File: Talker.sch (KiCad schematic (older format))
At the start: 61 parts, among them J1 DC_JACK, J2 DE9, J3 Audio Out, J4 TxE, J5 SPKR, J6 32/16, P1 10K, SW1 RESET, U1 CTS256A-AL2, U10 2732, U11 6116, U2 74ALS573, U3 74LS138, U4 SP0256A-AL2, U5 LM324, U6 LM386, U7 MAX232, U8 74LS14, Y1 10MHz, Y2 3.12MHz

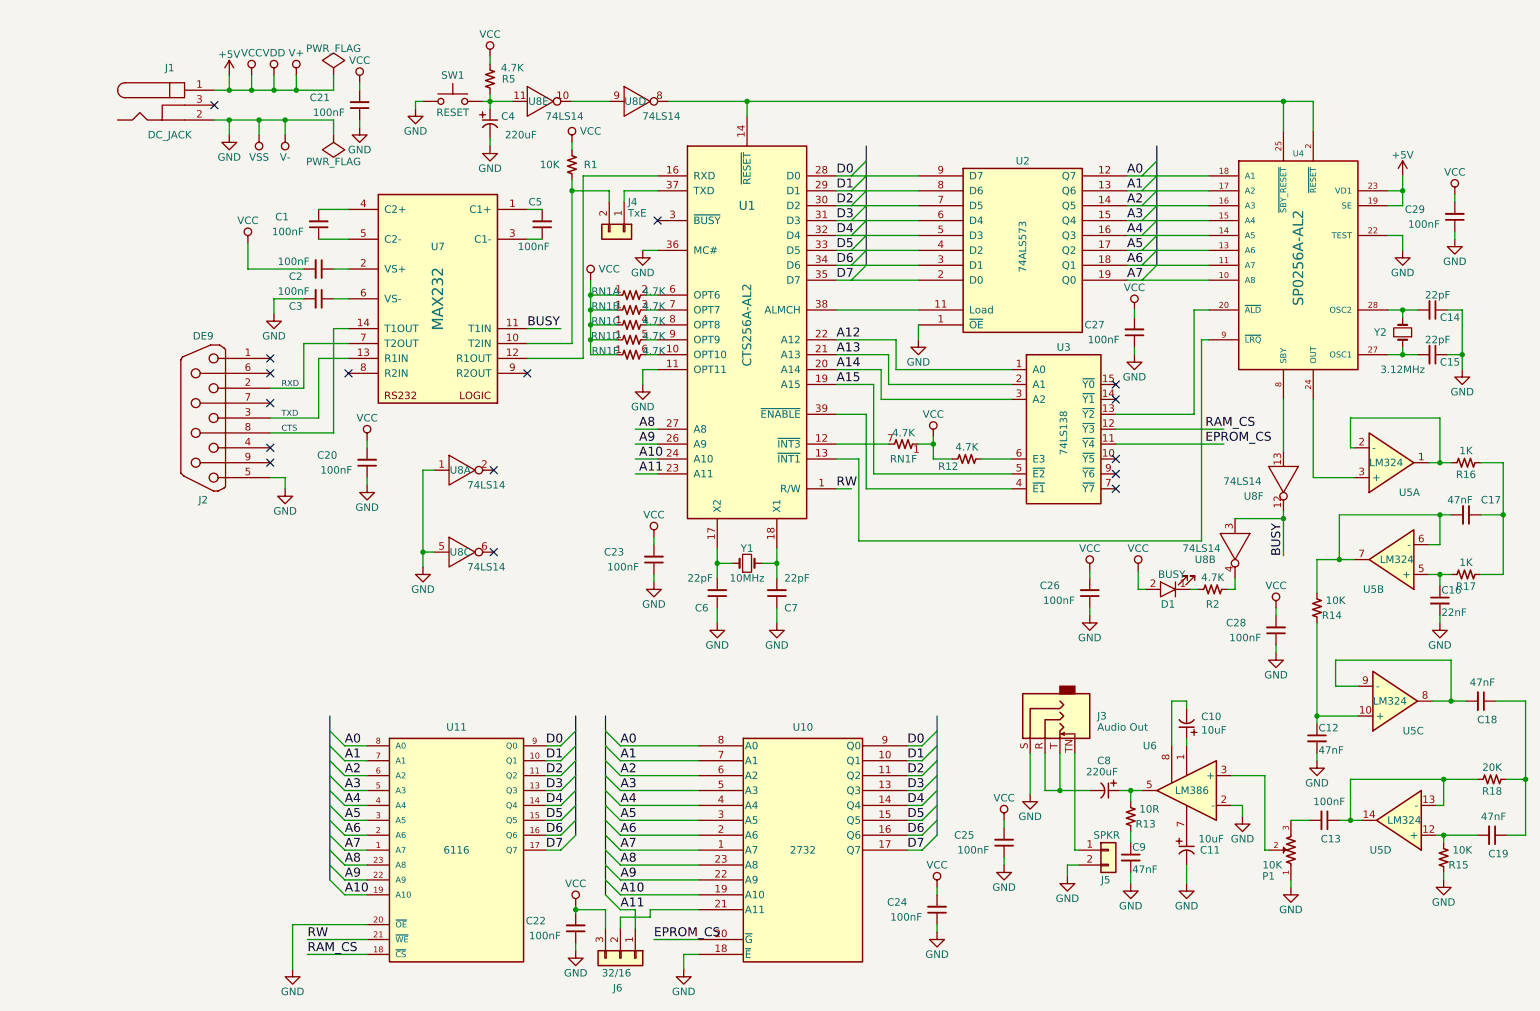
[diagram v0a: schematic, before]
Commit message: Modified the circuit to add a negative supply for the op-amp. It made a world of difference!
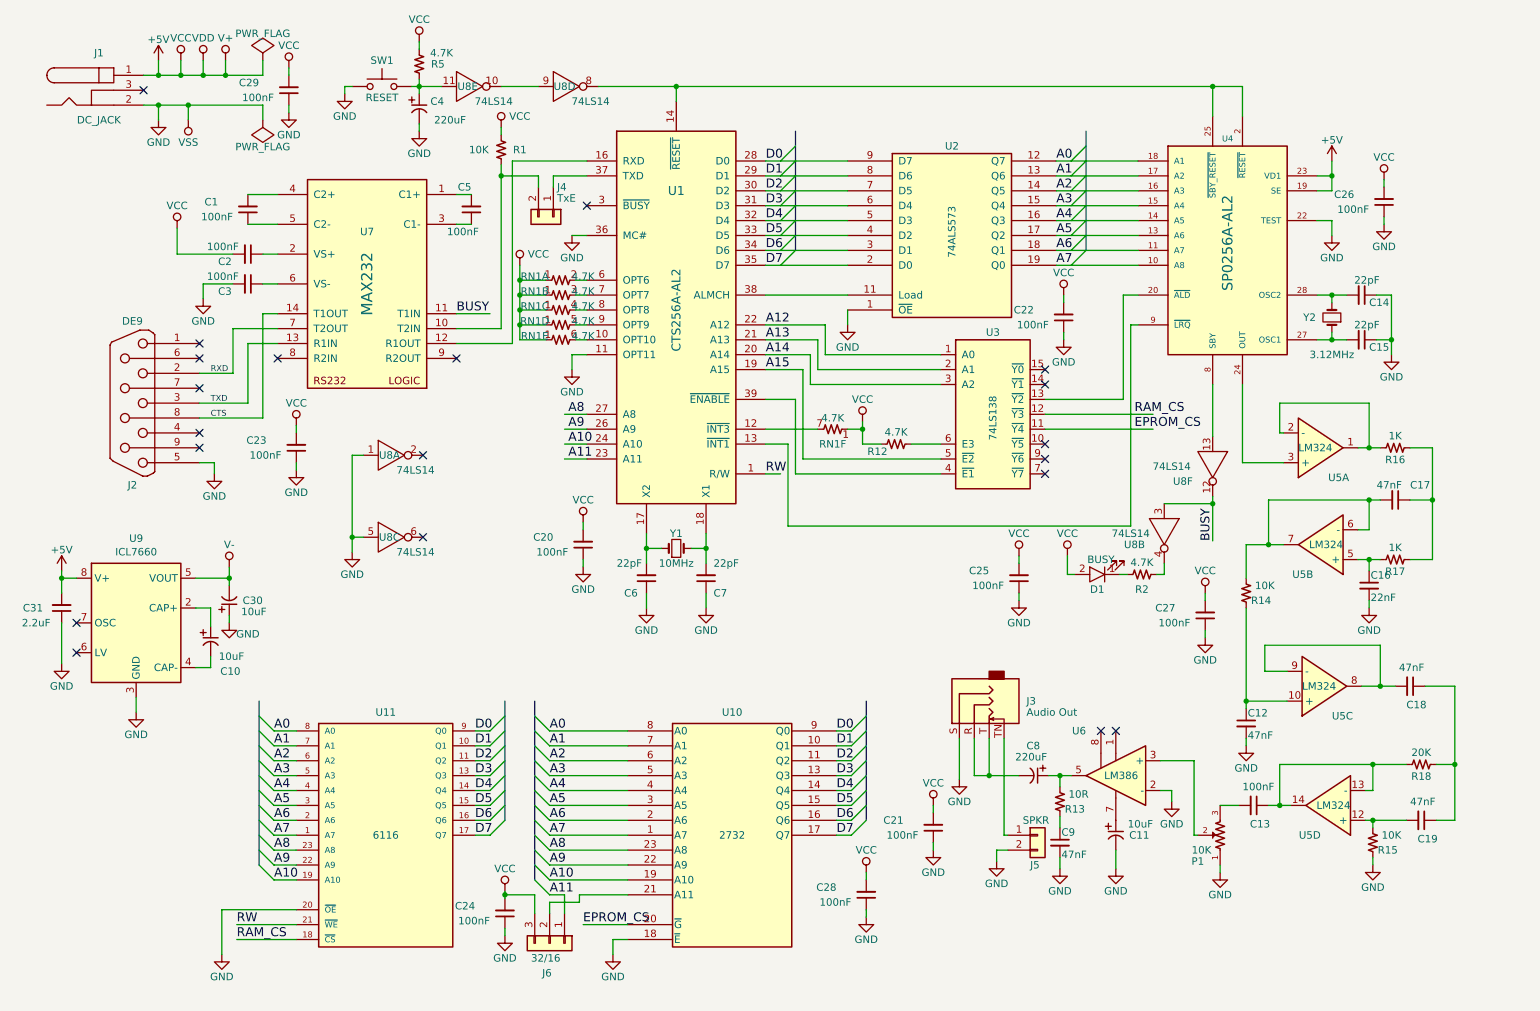
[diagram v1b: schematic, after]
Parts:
- added C30: 10uF, modules:CP_Radial_D5.0mm_P2.00mm, symbol Talker:CP_US
- added C31: 2.2uF, modules:C_Disc_D3_P2.5, symbol Talker:C_Small
- added U9: ICL7660, modules:DIP-8_W7.62mm_LongPads, symbol Talker:ICL7660
- renumbered C23 to C20, C25 to C21, C27 to C22, C20 to C23, C22 to C24, C26 to C25, C29 to C26, C28 to C27, C24 to C28, C21 to C29
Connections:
- wire segments 326 -> 333
- no-connect marks 16 -> 20
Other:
- moved on the sheet: C1, C11, C12, C13, C14, C15, C16, C17, C18, C19, C2, C20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
